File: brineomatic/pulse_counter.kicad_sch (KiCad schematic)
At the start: 7 parts

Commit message: updated resistor p/ns in bom
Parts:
- R5: LCSC (none) -> C22765
- R6: LCSC (none) -> C4190
- R7: LCSC (none) -> C23162
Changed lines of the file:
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@@
 			)
 		)
-		(property "LCSC" ""
+		(property "LCSC" " C23162"
 			(at 135.89 101.6 0)
 			(effects
@@
 			)
 		)
-		(property "LCSC" ""
+		(property "LCSC" "C22765"
 			(at 123.19 97.79 0)
 			(effects
@@
 			)
 		)
-		(property "LCSC" ""
+		(property "LCSC" " C4190"
 			(at 123.19 105.41 0)
 			(effects

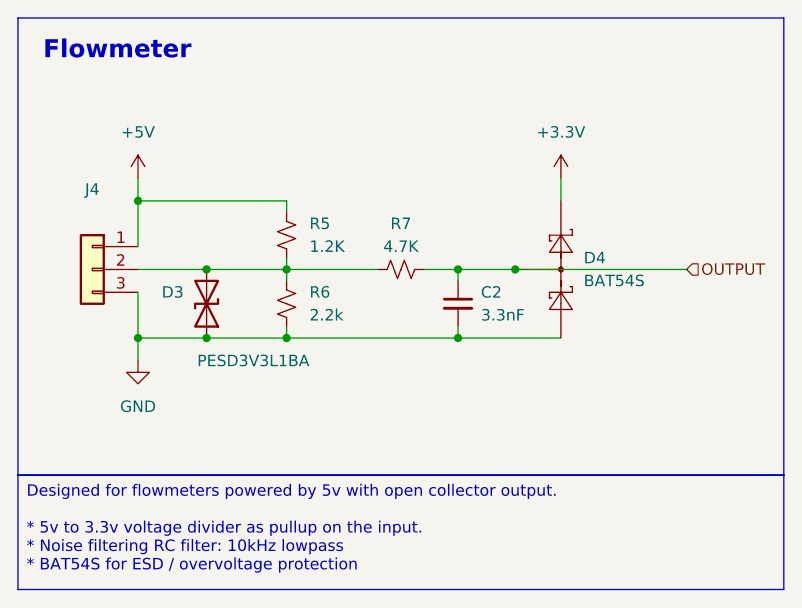
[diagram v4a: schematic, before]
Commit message: updated analog sensor esd schematic
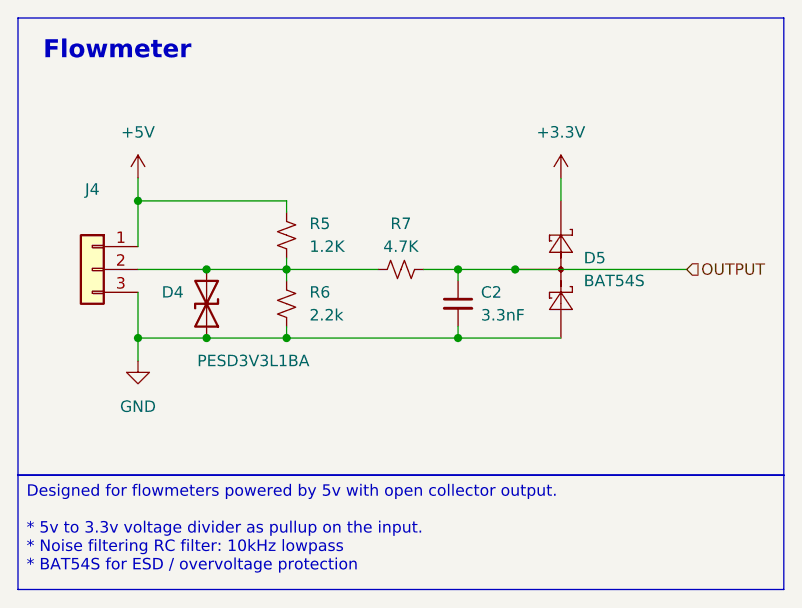
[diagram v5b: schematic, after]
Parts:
- renumbered D3 to D4, D4 to D5
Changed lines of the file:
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@@
 		(dnp no)
 		(fields_autoplaced yes)
-		(property "Reference" "#PWR013"
+		(property "Reference" "#PWR014"
 			(at 106.68 118.11 0)
 			(effects
@@
 			(project "brineomatic"
 				(path "/96477ae2-ef08-48f3-8dd4-fe4478541f68/afb25a63-7dc0-4ba4-a0ca-4f0b83c59f3b"
-					(reference "#PWR013")
-					(unit 1)
-				)
-				(path "/96477ae2-ef08-48f3-8dd4-fe4478541f68/c28d9395-3f2f-46b5-bdab-c14b6c7c5c4b"
-					(reference "#PWR033")
+					(reference "#PWR014")
+					(unit 1)
+				)
+				(path "/96477ae2-ef08-48f3-8dd4-fe4478541f68/c28d9395-3f2f-46b5-bdab-c14b6c7c5c4b"
+					(reference "#PWR034")
 					(unit 1)
 				)
@@
 		(dnp no)
 		(fields_autoplaced yes)
-		(property "Reference" "#PWR014"
+		(property "Reference" "#PWR015"
 			(at 153.67 95.25 0)
 			(effects
@@
 			(project "brineomatic"
 				(path "/96477ae2-ef08-48f3-8dd4-fe4478541f68/afb25a63-7dc0-4ba4-a0ca-4f0b83c59f3b"
-					(reference "#PWR014")
-					(unit 1)
-				)
-				(path "/96477ae2-ef08-48f3-8dd4-fe4478541f68/c28d9395-3f2f-46b5-bdab-c14b6c7c5c4b"
-					(reference "#PWR034")
+					(reference "#PWR015")
+					(unit 1)
+				)
+				(path "/96477ae2-ef08-48f3-8dd4-fe4478541f68/c28d9395-3f2f-46b5-bdab-c14b6c7c5c4b"
+					(reference "#PWR035")
 					(unit 1)
 				)
@@
 		(dnp no)
 		(fields_autoplaced yes)
-		(property "Reference" "D4"
+		(property "Reference" "D5"
 			(at 156.21 100.33 90)
 			(effects
@@
 			(project "brineomatic"
 				(path "/96477ae2-ef08-48f3-8dd4-fe4478541f68/afb25a63-7dc0-4ba4-a0ca-4f0b83c59f3b"
-					(reference "D4")
-					(unit 1)
-				)
-				(path "/96477ae2-ef08-48f3-8dd4-fe4478541f68/c28d9395-3f2f-46b5-bdab-c14b6c7c5c4b"
-					(reference "D24")
+					(reference "D5")
+					(unit 1)
+				)
+				(path "/96477ae2-ef08-48f3-8dd4-fe4478541f68/c28d9395-3f2f-46b5-bdab-c14b6c7c5c4b"
+					(reference "D25")
 					(unit 1)
 				)
@@
 		(dnp no)
 		(fields_autoplaced yes)
-		(property "Reference" "#PWR012"
+		(property "Reference" "#PWR013"
 			(at 106.68 95.25 0)
 			(effects
@@
 			(project ""
 				(path "/96477ae2-ef08-48f3-8dd4-fe4478541f68/afb25a63-7dc0-4ba4-a0ca-4f0b83c59f3b"
-					(reference "#PWR012")
-					(unit 1)
-				)
-				(path "/96477ae2-ef08-48f3-8dd4-fe4478541f68/c28d9395-3f2f-46b5-bdab-c14b6c7c5c4b"
-					(reference "#PWR032")
+					(reference "#PWR013")
+					(unit 1)
+				)
+				(path "/96477ae2-ef08-48f3-8dd4-fe4478541f68/c28d9395-3f2f-46b5-bdab-c14b6c7c5c4b"
+					(reference "#PWR033")
 					(unit 1)
 				)
@@
 		(on_board yes)
 		(dnp no)
-		(property "Reference" "D3"
+		(property "Reference" "D4"
 			(at 111.76 104.1399 90)
 			(effects
@@
 			(project "brineomatic"
 				(path "/96477ae2-ef08-48f3-8dd4-fe4478541f68/afb25a63-7dc0-4ba4-a0ca-4f0b83c59f3b"
-					(reference "D3")
-					(unit 1)
-				)
-				(path "/96477ae2-ef08-48f3-8dd4-fe4478541f68/c28d9395-3f2f-46b5-bdab-c14b6c7c5c4b"
-					(reference "D23")
-					(unit 1)
-				)
+					(reference "D4")
+					(unit 1)
+				)
+				(path "/96477ae2-ef08-48f3-8dd4-fe4478541f68/c28d9395-3f2f-46b5-bdab-c14b6c7c5c4b"
+					(reference "D24")
+					(unit 1)
+				)

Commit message: added bulk cap after ideal diode
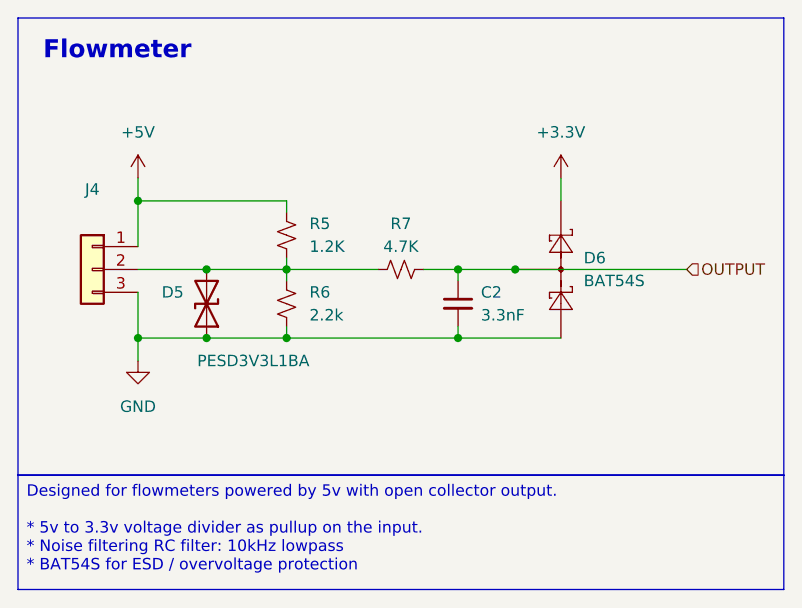
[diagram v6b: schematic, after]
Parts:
- renumbered D4 to D5, D5 to D6
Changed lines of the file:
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@@
 		(dnp no)
 		(fields_autoplaced yes)
-		(property "Reference" "#PWR014"
+		(property "Reference" "#PWR016"
 			(at 106.68 118.11 0)
 			(effects
@@
 			(project "brineomatic"
 				(path "/96477ae2-ef08-48f3-8dd4-fe4478541f68/afb25a63-7dc0-4ba4-a0ca-4f0b83c59f3b"
-					(reference "#PWR014")
-					(unit 1)
-				)
-				(path "/96477ae2-ef08-48f3-8dd4-fe4478541f68/c28d9395-3f2f-46b5-bdab-c14b6c7c5c4b"
-					(reference "#PWR034")
+					(reference "#PWR016")
+					(unit 1)
+				)
+				(path "/96477ae2-ef08-48f3-8dd4-fe4478541f68/c28d9395-3f2f-46b5-bdab-c14b6c7c5c4b"
+					(reference "#PWR036")
 					(unit 1)
 				)
@@
 		(dnp no)
 		(fields_autoplaced yes)
-		(property "Reference" "#PWR015"
+		(property "Reference" "#PWR017"
 			(at 153.67 95.25 0)
 			(effects
@@
 			(project "brineomatic"
 				(path "/96477ae2-ef08-48f3-8dd4-fe4478541f68/afb25a63-7dc0-4ba4-a0ca-4f0b83c59f3b"
-					(reference "#PWR015")
-					(unit 1)
-				)
-				(path "/96477ae2-ef08-48f3-8dd4-fe4478541f68/c28d9395-3f2f-46b5-bdab-c14b6c7c5c4b"
-					(reference "#PWR035")
+					(reference "#PWR017")
+					(unit 1)
+				)
+				(path "/96477ae2-ef08-48f3-8dd4-fe4478541f68/c28d9395-3f2f-46b5-bdab-c14b6c7c5c4b"
+					(reference "#PWR037")
 					(unit 1)
 				)
@@
 		(dnp no)
 		(fields_autoplaced yes)
-		(property "Reference" "D5"
+		(property "Reference" "D6"
 			(at 156.21 100.33 90)
 			(effects
@@
 			(project "brineomatic"
 				(path "/96477ae2-ef08-48f3-8dd4-fe4478541f68/afb25a63-7dc0-4ba4-a0ca-4f0b83c59f3b"
-					(reference "D5")
-					(unit 1)
-				)
-				(path "/96477ae2-ef08-48f3-8dd4-fe4478541f68/c28d9395-3f2f-46b5-bdab-c14b6c7c5c4b"
-					(reference "D25")
+					(reference "D6")
+					(unit 1)
+				)
+				(path "/96477ae2-ef08-48f3-8dd4-fe4478541f68/c28d9395-3f2f-46b5-bdab-c14b6c7c5c4b"
+					(reference "D24")
 					(unit 1)
 				)
@@
 		(dnp no)
 		(fields_autoplaced yes)
-		(property "Reference" "#PWR013"
+		(property "Reference" "#PWR015"
 			(at 106.68 95.25 0)
 			(effects
@@
 			(project ""
 				(path "/96477ae2-ef08-48f3-8dd4-fe4478541f68/afb25a63-7dc0-4ba4-a0ca-4f0b83c59f3b"
-					(reference "#PWR013")
-					(unit 1)
-				)
-				(path "/96477ae2-ef08-48f3-8dd4-fe4478541f68/c28d9395-3f2f-46b5-bdab-c14b6c7c5c4b"
-					(reference "#PWR033")
+					(reference "#PWR015")
+					(unit 1)
+				)
+				(path "/96477ae2-ef08-48f3-8dd4-fe4478541f68/c28d9395-3f2f-46b5-bdab-c14b6c7c5c4b"
+					(reference "#PWR035")
 					(unit 1)
 				)
@@
 		(on_board yes)
 		(dnp no)
-		(property "Reference" "D4"
+		(property "Reference" "D5"
 			(at 111.76 104.1399 90)
 			(effects
@@
 			(project "brineomatic"
 				(path "/96477ae2-ef08-48f3-8dd4-fe4478541f68/afb25a63-7dc0-4ba4-a0ca-4f0b83c59f3b"
-					(reference "D4")
-					(unit 1)
-				)
-				(path "/96477ae2-ef08-48f3-8dd4-fe4478541f68/c28d9395-3f2f-46b5-bdab-c14b6c7c5c4b"
-					(reference "D24")
+					(reference "D5")
+					(unit 1)
+				)
+				(path "/96477ae2-ef08-48f3-8dd4-fe4478541f68/c28d9395-3f2f-46b5-bdab-c14b6c7c5c4b"
+					(reference "D23")
 					(unit 1)
 				)
@@
 				)
 				(path "/96477ae2-ef08-48f3-8dd4-fe4478541f68/c28d9395-3f2f-46b5-bdab-c14b6c7c5c4b"
-					(reference "C18")
-					(unit 1)
-				)
+					(reference "C20")
+					(unit 1)
+				)

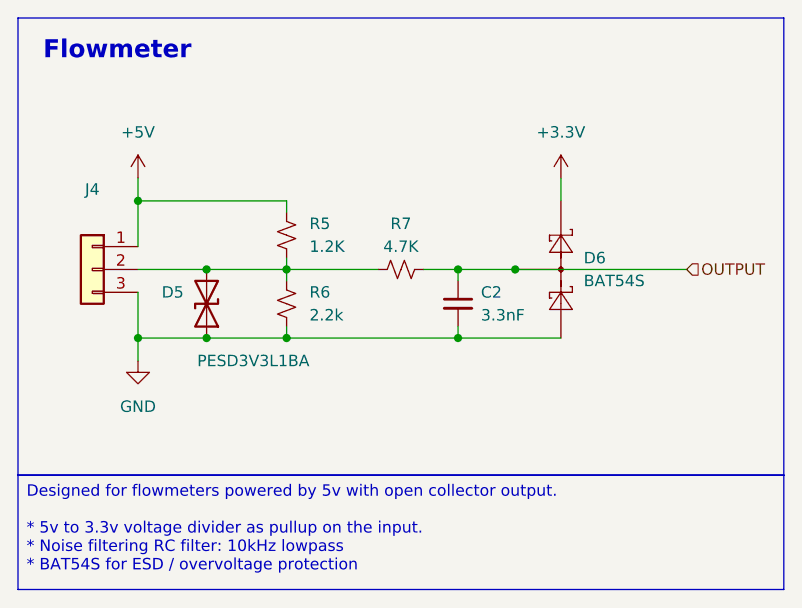
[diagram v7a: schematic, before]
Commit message: added 1uF cap to pressure sensor connectors for esd
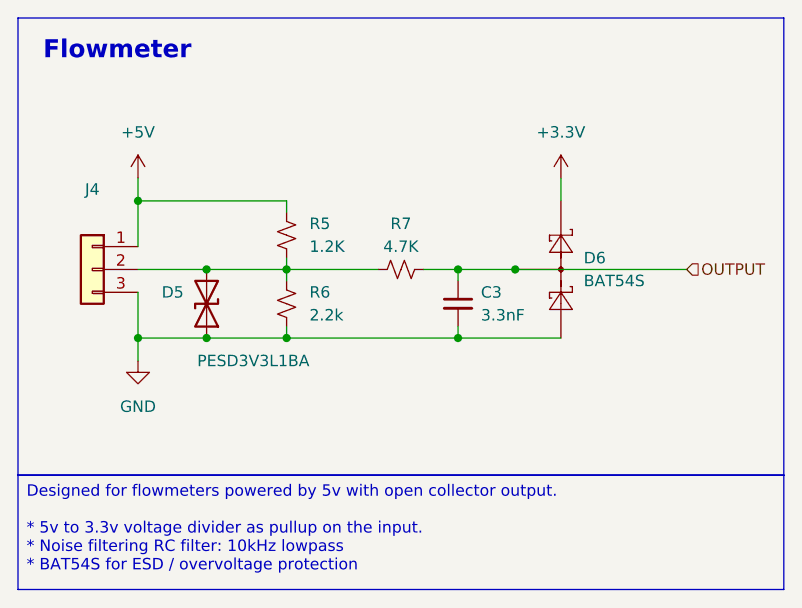
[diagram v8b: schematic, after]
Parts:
- renumbered C2 to C3
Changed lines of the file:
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@@
 		(dnp no)
 		(fields_autoplaced yes)
-		(property "Reference" "C2"
+		(property "Reference" "C3"
 			(at 144.78 104.1462 0)
 			(effects
@@
 			(project "brineomatic"
 				(path "/96477ae2-ef08-48f3-8dd4-fe4478541f68/afb25a63-7dc0-4ba4-a0ca-4f0b83c59f3b"
-					(reference "C2")
+					(reference "C3")
 					(unit 1)
 				)
 				(path "/96477ae2-ef08-48f3-8dd4-fe4478541f68/c28d9395-3f2f-46b5-bdab-c14b6c7c5c4b"
-					(reference "C22")
+					(reference "C23")
 					(unit 1)
 				)
